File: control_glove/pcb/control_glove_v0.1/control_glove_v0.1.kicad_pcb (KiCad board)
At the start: 2 copper layers, 20 parts, among them P1 Power_Pins, Q1 Q_NPN_ECB, SW1 SW_Push, SW2 SW_Push, U1 UART-RF433

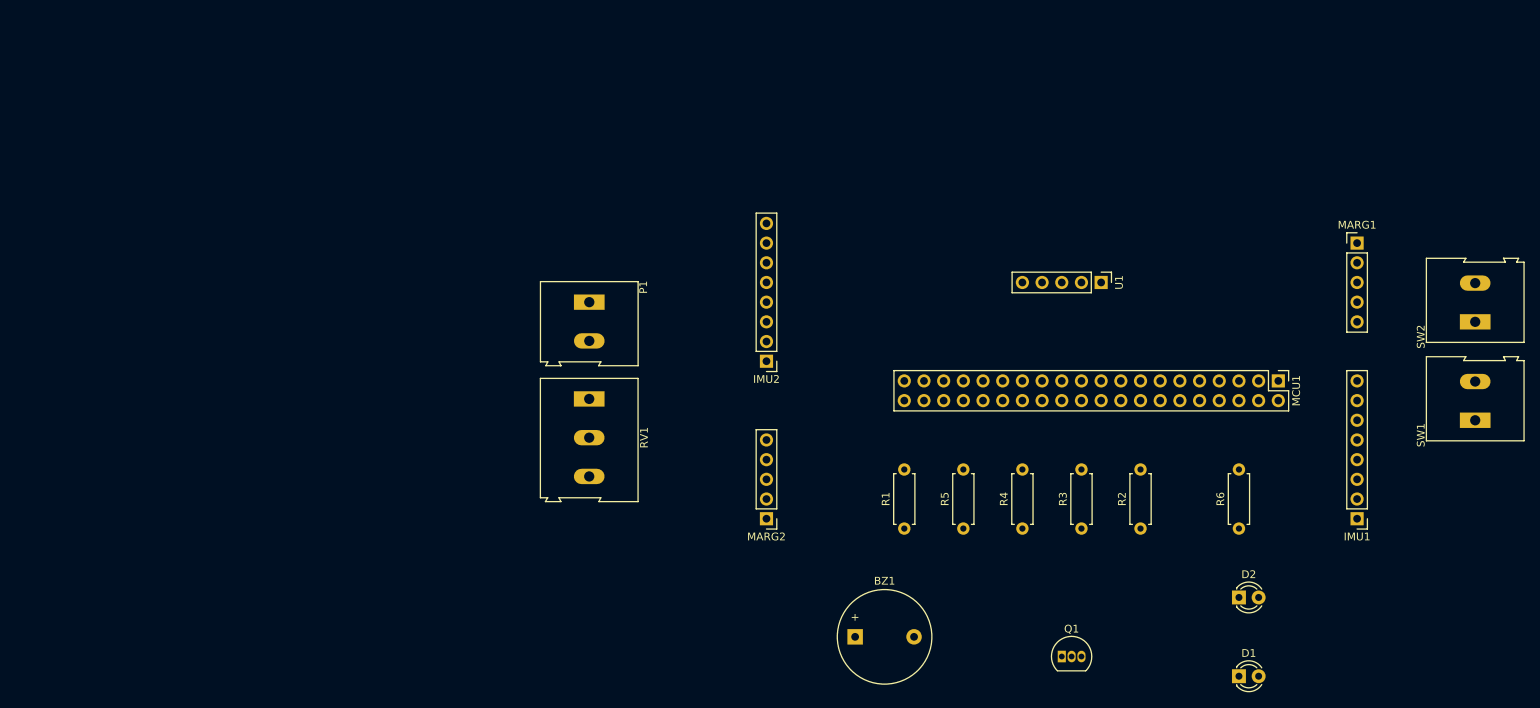
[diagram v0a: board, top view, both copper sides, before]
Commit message: update: PCB setup and arange component positions
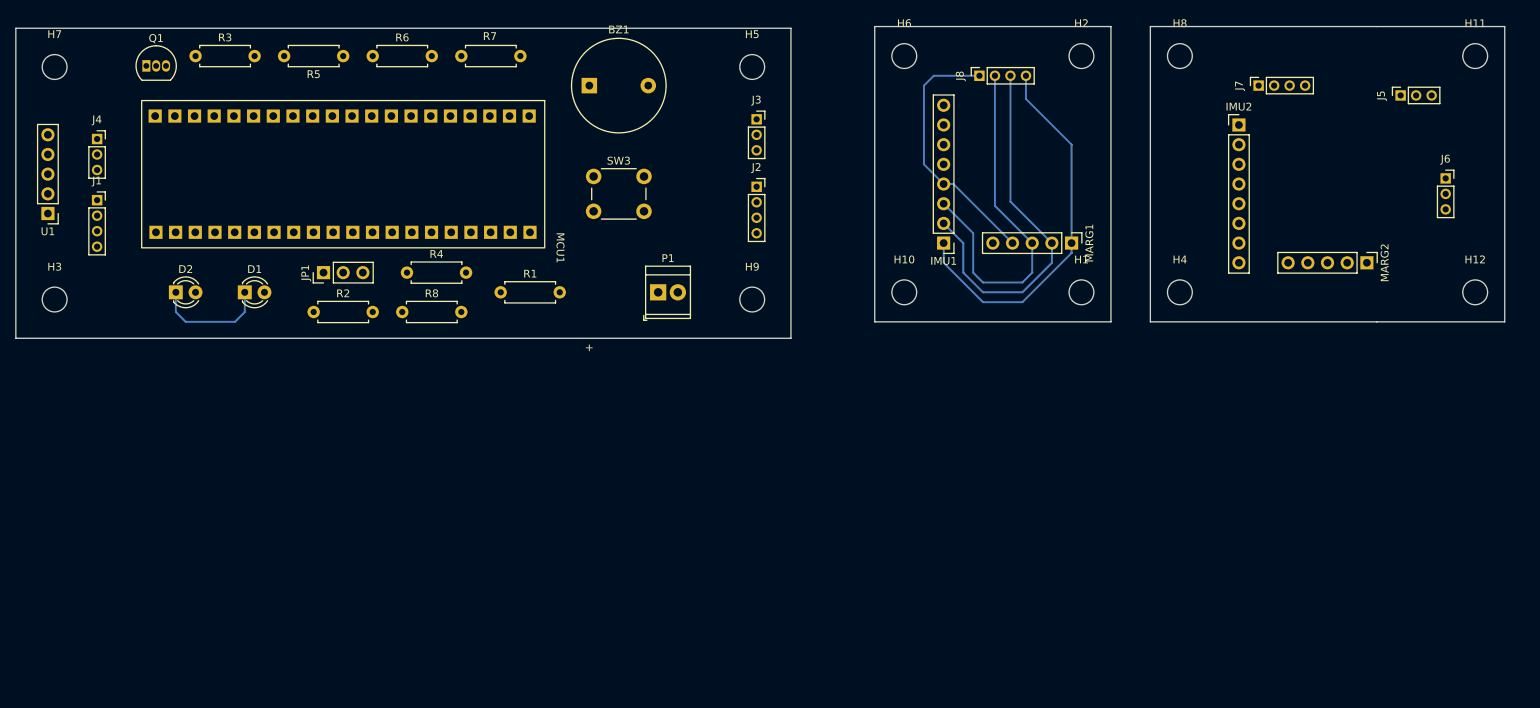
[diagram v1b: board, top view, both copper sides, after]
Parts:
- removed RV1: 10K, TerminalBlock:TerminalBlock_Altech_AK300-3_P5.00mm
- removed SW1, SW2: SW_Push, TerminalBlock:TerminalBlock_Altech_AK300-2_P5.00mm
- added H1: MountingHole, MountingHole:MountingHole_3.2mm_M3, F.Cu at (157.5, 52.1)
- added H10: MountingHole, MountingHole:MountingHole_3.2mm_M3, F.Cu at (134.6, 52.1)
- added H11: MountingHole, MountingHole:MountingHole_3.2mm_M3, F.Cu at (208.3, 21.6)
- added H12: MountingHole, MountingHole:MountingHole_3.2mm_M3, F.Cu at (208.3, 52.1)
- added H2: MountingHole, MountingHole:MountingHole_3.2mm_M3, F.Cu at (157.5, 21.6)
- added H3: MountingHole, MountingHole:MountingHole_3.2mm_M3, F.Cu at (25.0, 53.0)
- added H4: MountingHole, MountingHole:MountingHole_3.2mm_M3, F.Cu at (170.2, 52.1)
- added H5: MountingHole, MountingHole:MountingHole_3.2mm_M3, F.Cu at (115.0, 23.0)
- added H6: MountingHole, MountingHole:MountingHole_3.2mm_M3, F.Cu at (134.6, 21.6)
- added H7: MountingHole, MountingHole:MountingHole_3.2mm_M3, F.Cu at (25.0, 23.0)
- added H8: MountingHole, MountingHole:MountingHole_3.2mm_M3, F.Cu at (170.2, 21.6)
- added H9: MountingHole, MountingHole:MountingHole_3.2mm_M3, F.Cu at (115.0, 53.0)
- added J1: Conn_01x04_Female, Connector_PinSocket_2.00mm:PinSocket_1x04_P2.00mm_Vertical, F.Cu at (30.5, 40.2)
- added J2: Conn_01x04_Female, Connector_PinSocket_2.00mm:PinSocket_1x04_P2.00mm_Vertical, F.Cu at (115.6, 38.5)
- added J3: Conn_01x03_Female, Connector_PinSocket_2.00mm:PinSocket_1x03_P2.00mm_Vertical, F.Cu at (115.6, 29.8)
- added J4: Conn_01x03_Female, Connector_PinSocket_2.00mm:PinSocket_1x03_P2.00mm_Vertical, F.Cu at (30.5, 32.3)
- added J5: Conn_01x03_Female, Connector_PinSocket_2.00mm:PinSocket_1x03_P2.00mm_Vertical, F.Cu at (198.7, 26.7)
- added J6: Conn_01x03_Female, Connector_PinSocket_2.00mm:PinSocket_1x03_P2.00mm_Vertical, F.Cu at (204.5, 37.4)
- added J7: Conn_01x04_Female, Connector_PinSocket_2.00mm:PinSocket_1x04_P2.00mm_Vertical, F.Cu at (180.3, 25.4)
- added J8: Conn_01x04_Female, Connector_PinSocket_2.00mm:PinSocket_1x04_P2.00mm_Vertical, F.Cu at (144.3, 24.1)
- added JP1: Jumper_3_Bridged12, Connector_PinHeader_2.54mm:PinHeader_1x03_P2.54mm_Vertical, F.Cu at (59.7, 49.5)
- added R7: 1K, Resistor_THT:R_Axial_DIN0207_L6.3mm_D2.5mm_P7.62mm_Horizontal, F.Cu at (77.5, 21.6)
- added R8: 300, Resistor_THT:R_Axial_DIN0207_L6.3mm_D2.5mm_P7.62mm_Horizontal, F.Cu at (69.8, 54.6)
- added SW3: SW_Push, Button_Switch_THT:SW_PUSH_6mm_H13mm, F.Cu at (94.5, 37.1)
- MCU1: footprint Connector_PinHeader_2.54mm:PinHeader_2x20_P2.54mm_Vertical -> hieu:stm32f4_board
- P1: footprint TerminalBlock:TerminalBlock_Altech_AK300-2_P5.00mm -> TerminalBlock_TE-Connectivity:TerminalBlock_TE_282834-2_1x02_P2.54mm_Horizontal
- moved D2 142.7 mm to (40.6, 52.1)
- moved Q1 140.6 mm to (36.8, 22.9)
- moved D1 137.5 mm to (49.5, 52.1)
- moved U1 136.2 mm to (24.1, 41.9), turned to 180 degrees
- moved R3 129.5 mm to (43.2, 21.6), turned to 0 degrees
- moved R6 127.3 mm to (66.0, 21.6), turned to 0 degrees
- moved R2 110.3 mm to (58.4, 54.6), turned to 0 degrees
- moved MCU1 102.5 mm to (86.2, 29.3)
- moved R5 100.6 mm to (62.2, 21.6), turned to 180 degrees
- moved R4 86.0 mm to (70.5, 49.5), turned to 0 degrees
- moved MARG2 84.2 mm to (194.3, 48.3), turned to -90 degrees
- moved BZ1 79.0 mm to (94.0, 25.4)
- moved IMU2 68.2 mm to (177.8, 30.5), turned to 0 degrees
- moved IMU1 64.1 mm to (139.7, 45.7)
- moved R1 60.3 mm to (82.5, 52.1), turned to 0 degrees
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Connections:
- BZ1 pad 1: BUZZER -> Net-(BZ1-Pad1)
- IMU1 pad 1: SENSOR-3.3V -> Net-(IMU1-Pad1)
- IMU1 pad 2: SENSOR-GND -> Net-(IMU1-Pad2)
- IMU1 pad 3: SCL1 -> Net-(IMU1-Pad3)
- IMU1 pad 4: SDA1 -> Net-(IMU1-Pad4)
- IMU2 pad 1: SENSOR-3.3V -> Net-(IMU2-Pad1)
- IMU2 pad 2: SENSOR-GND -> Net-(IMU2-Pad2)
- IMU2 pad 3: SCL2 -> Net-(IMU2-Pad3)
- IMU2 pad 4: SDA2 -> Net-(IMU2-Pad4)
- MARG1 pad 1: SENSOR-3.3V -> Net-(IMU1-Pad1)
- MARG1 pad 2: SENSOR-GND -> Net-(IMU1-Pad2)
- MARG1 pad 3: SCL1 -> Net-(IMU1-Pad3)
- MARG1 pad 4: SDA1 -> Net-(IMU1-Pad4)
- MARG2 pad 1: SENSOR-3.3V -> Net-(IMU2-Pad1)
- MARG2 pad 2: SENSOR-GND -> Net-(IMU2-Pad2)
- MARG2 pad 3: SCL2 -> Net-(IMU2-Pad3)
- MARG2 pad 4: SDA2 -> Net-(IMU2-Pad4)
- MCU1 pad 32: unconnected-(MCU1-Pad32) -> SW3
- Q1 pad 2: SENSOR-GND -> Net-(Q1-Pad2)
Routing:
- net Net-(IMU1-Pad1): track 0.00 -> 49.1 mm
- net Net-(IMU1-Pad2): track 0.00 -> 47.8 mm
- net Net-(IMU1-Pad3): track 0.00 -> 46.5 mm
- net Net-(IMU1-Pad4): track 0.00 -> 33.5 mm
- net GND: track 0.00 -> 15.0 mm
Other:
- board outline added: 192.1 x 40.2 mm

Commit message: update: Complete connect all components on PCB
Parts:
- added R10: 0, Resistor_THT:R_Axial_DIN0207_L6.3mm_D2.5mm_P7.62mm_Horizontal, F.Cu at (100.2, 38.0)
- added R11: 0, Resistor_THT:R_Axial_DIN0207_L6.3mm_D2.5mm_P7.62mm_Horizontal, F.Cu at (70.9, 24.3)
- added R12: 0, Resistor_THT:R_Axial_DIN0207_L6.3mm_D2.5mm_P7.62mm_Horizontal, F.Cu at (111.6, 33.5)
- added R13: 0, Resistor_THT:R_Axial_DIN0207_L6.3mm_D2.5mm_P7.62mm_Horizontal, F.Cu at (55.8, 51.9)
- added R14: 0, Resistor_THT:R_Axial_DIN0207_L6.3mm_D2.5mm_P7.62mm_Horizontal, F.Cu at (46.0, 51.9)
- added R9: 0, Resistor_THT:R_Axial_DIN0207_L6.3mm_D2.5mm_P7.62mm_Horizontal, F.Cu at (43.3, 32.4)
- moved J2 87.9 mm to (28.1, 30.2), turned to 180 degrees
- moved J3 87.5 mm to (28.2, 34.3)
- moved J1 87.0 mm to (116.8, 30.0)
- moved J4 86.8 mm to (116.8, 41.5)
- moved Q1 57.4 mm to (87.1, 50.6), turned to 180 degrees
- moved H11 57.2 mm to (265.4, 20.3)
- moved H12 57.2 mm to (265.4, 50.8)
- moved J5 57.2 mm to (255.8, 25.4)
- moved J6 57.2 mm to (261.6, 36.1)
- moved J7 57.2 mm to (237.5, 24.1)
- moved IMU2 56.4 mm to (232.4, 44.5), turned to 180 degrees
- moved MARG2 54.5 mm to (248.7, 44.3)
- moved D2 50.1 mm to (80.8, 22.2)
- moved R5 48.9 mm to (108.3, 38.0), turned to -90 degrees
- moved D1 48.8 mm to (88.1, 22.2)
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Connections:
- J1 pad 1: SENSOR-3.3V -> 3.3V-SHOULDER
- J2 pad 1: SENSOR-3.3V -> 3.3V
- J2 pad 4: SENSOR-GND -> Net-(R11-Pad2)
- JP1 pad 1: SENSOR-GND -> Net-(JP1-Pad1)
- MCU1 pad 23: SENSOR-3.3V -> 3.3V-SHOULDER
- R5 pad 1: 3.3V -> 3.3V-SHOULDER
- U1 pad 1: 5V -> Net-(R9-Pad2)
- U1 pad 5: SET_UART -> Net-(U1-Pad5)
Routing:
- net GND: track 15.0 -> 318.1 mm
- net TX: track 0.00 -> 98.4 mm
- net RV1: track 0.00 -> 92.9 mm
- net RX: track 0.00 -> 88.2 mm
- net SDA1: track 0.00 -> 69.2 mm
- net SCL2: track 0.00 -> 69.2 mm
- net Net-(IMU2-Pad2): track 0.00 -> 66.2 mm
- net SCL1: track 0.00 -> 65.4 mm
- net SDA2: track 0.00 -> 51.6 mm
- net Net-(IMU2-Pad3): track 0.00 -> 49.7 mm
- net Net-(R11-Pad1): track 0.00 -> 48.3 mm
- net Net-(D2-Pad2): track 0.00 -> 46.2 mm
- net 3.3V-SHOULDER: track 0.00 -> 44.7 mm
- net Net-(IMU2-Pad1): track 0.00 -> 42.7 mm
- net Net-(D1-Pad2): track 0.00 -> 36.7 mm
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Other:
- board size 192.1 x 40.2 mm -> 253.2 x 47 mm

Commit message: update: Complete fix pcb
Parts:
- SW3: footprint Button_Switch_THT:SW_PUSH_6mm_H13mm -> Resistor_THT:R_Axial_DIN0207_L6.3mm_D2.5mm_P7.62mm_Horizontal
- moved H11 100.5 mm to (174.0, 62.0)
- moved J6 86.6 mm to (175.0, 34.0)
- moved J5 76.8 mm to (179.0, 23.0)
- moved H1 64.2 mm to (131.0, 20.0)
- moved H12 60.5 mm to (206.0, 62.0)
- moved H2 49.7 mm to (163.0, 62.0)
- moved MARG2 49.2 mm to (201.0, 32.0), turned to 0 degrees
- moved H6 45.9 mm to (131.0, 62.0)
- moved J7 42.5 mm to (195.0, 23.0), turned to -90 degrees
- moved H8 36.8 mm to (174.0, 19.0)
- moved H10 34.3 mm to (163.0, 19.0)
- moved MARG1 33.3 mm to (155.2, 32.4), turned to 0 degrees
- moved H4 32.2 mm to (206.0, 19.0)
- moved IMU2 31.9 mm to (200.9, 49.0), turned to -90 degrees
- moved J8 27.8 mm to (147.0, 23.0), turned to -90 degrees
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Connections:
- JP1 pad 1: Net-(JP1-Pad1) -> GND
- JP1 pad 2: GND -> Net-(JP1-Pad2)
- R10 pad 2: Net-(JP1-Pad1) -> Net-(JP1-Pad2)
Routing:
- net Net-(IMU2-Pad1): track 42.7 -> 57.5 mm
- net Net-(IMU2-Pad2): track 66.2 -> 51.8 mm
- net Net-(IMU1-Pad2): track 65.0 -> 50.9 mm
- net GND: track 318.1 -> 331.5 mm
- net SDA2: track 51.6 -> 38.7 mm
- net Net-(IMU1-Pad1): track 46.2 -> 58.2 mm
- net SW3: track 35.6 -> 46.4 mm
- net Net-(JP1-Pad2): track 0.00 -> 9.75 mm
- net Net-(IMU1-Pad4): track 29.3 -> 36.4 mm
- net Net-(IMU1-Pad3): track 50.2 -> 44.6 mm
- net Net-(IMU2-Pad4): track 28.3 -> 33.4 mm
- net Net-(JP1-Pad1): track 4.68 -> 0.00 mm
- net Net-(IMU2-Pad3): track 49.7 -> 45.8 mm
- net Net-(Q1-Pad2): track 13.3 -> 10.7 mm
- net Net-(J5-Pad1): track 14.9 -> 12.7 mm
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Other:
- board size 253.2 x 47 mm -> 194 x 51 mm
